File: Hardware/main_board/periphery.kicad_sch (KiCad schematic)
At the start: 66 parts, among them J4 SD, J5 NFC, J6 EXT1, J7 EXT0, U12 LP5562TMX

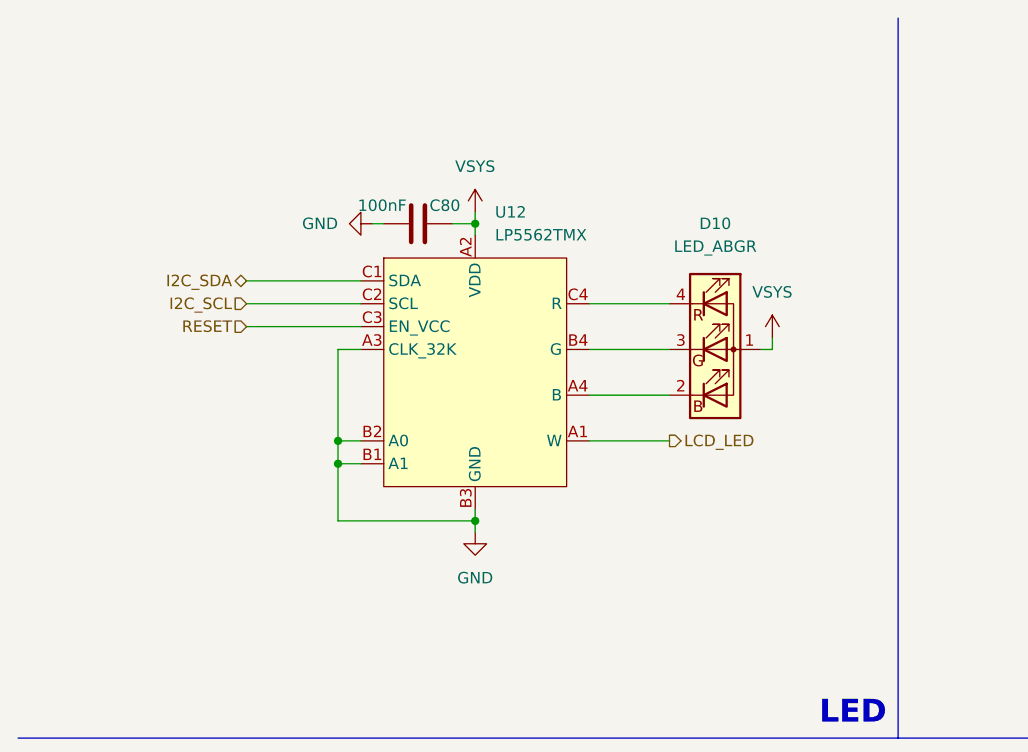
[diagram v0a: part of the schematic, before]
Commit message: change the Package of D10 to LTST-C19HE1WT
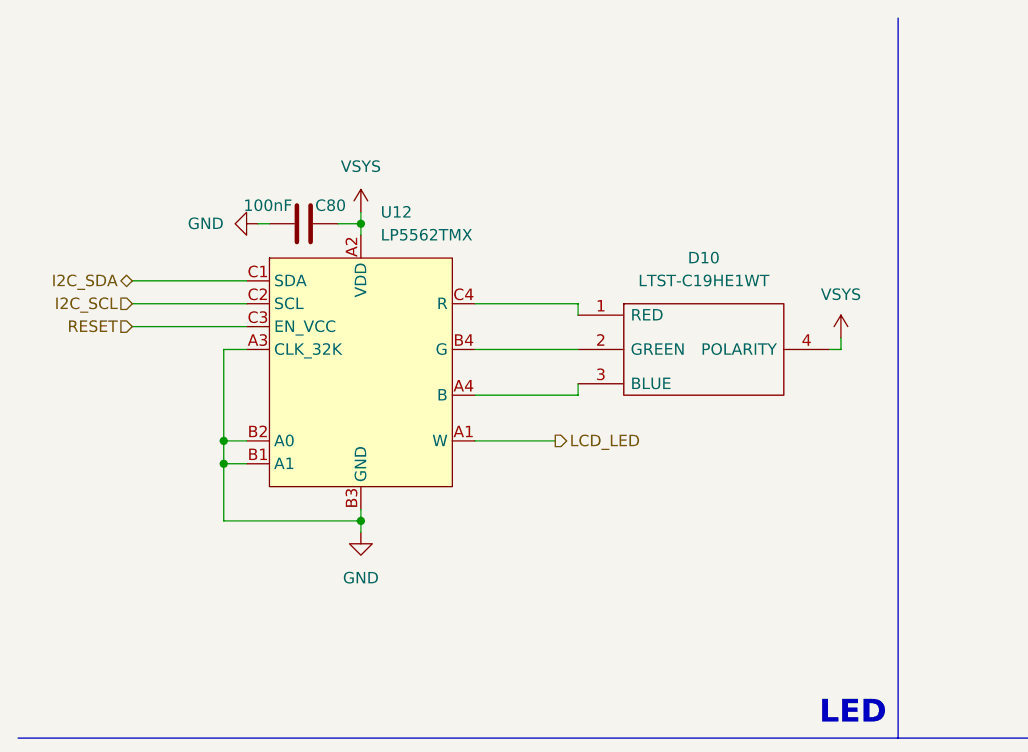
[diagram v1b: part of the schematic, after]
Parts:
- removed D10: LED_ABGR, Library:LED_PLCC-4_1.5x1.5mm_CW, symbol Device:LED_ABGR
- added D10: LTST-C19HE1WT, Library:LTST-C19HE1WT, symbol Library:LTST-C19HE1WT
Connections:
- net VSYS: now also D10.4 (POLARITY)
- net at U12.A4 (B): now also D10.3 (BLUE)
- net at U12.B4 (G): now also D10.2 (GREEN)
- net at U12.C4 (R): now also D10.1 (RED)
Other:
- moved on the sheet: C80, U12
